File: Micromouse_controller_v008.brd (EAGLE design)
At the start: 50.8 x 43.2 mm, 17 parts, among them IC2 TA4805BF, U1 ATMEGA328P_TQFP

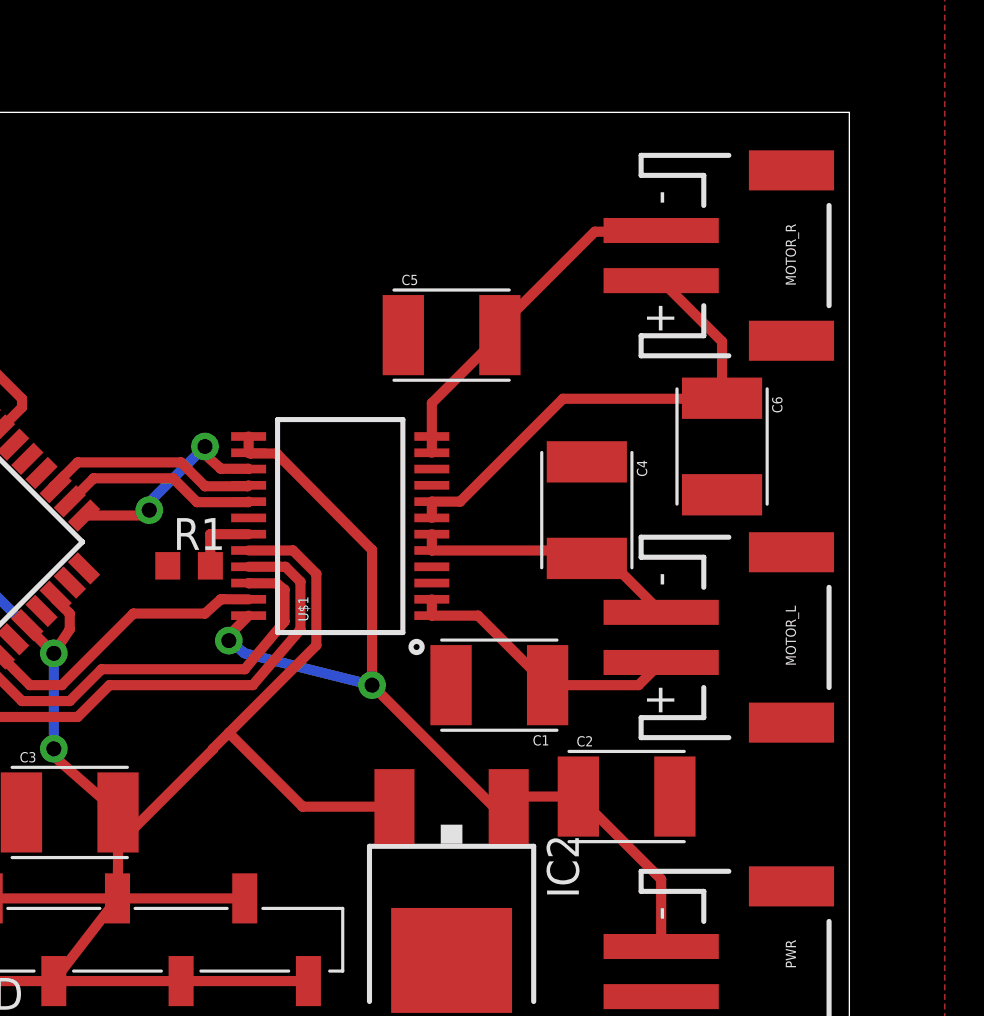
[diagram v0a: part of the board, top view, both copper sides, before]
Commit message: Version 1.0 of Micromouse controller 	Added capacitor values 	Arranged Labels 	Completed BoM and Presentation
Signed-off-by: Matthew Lumantas <mluma001@ucr.edu>
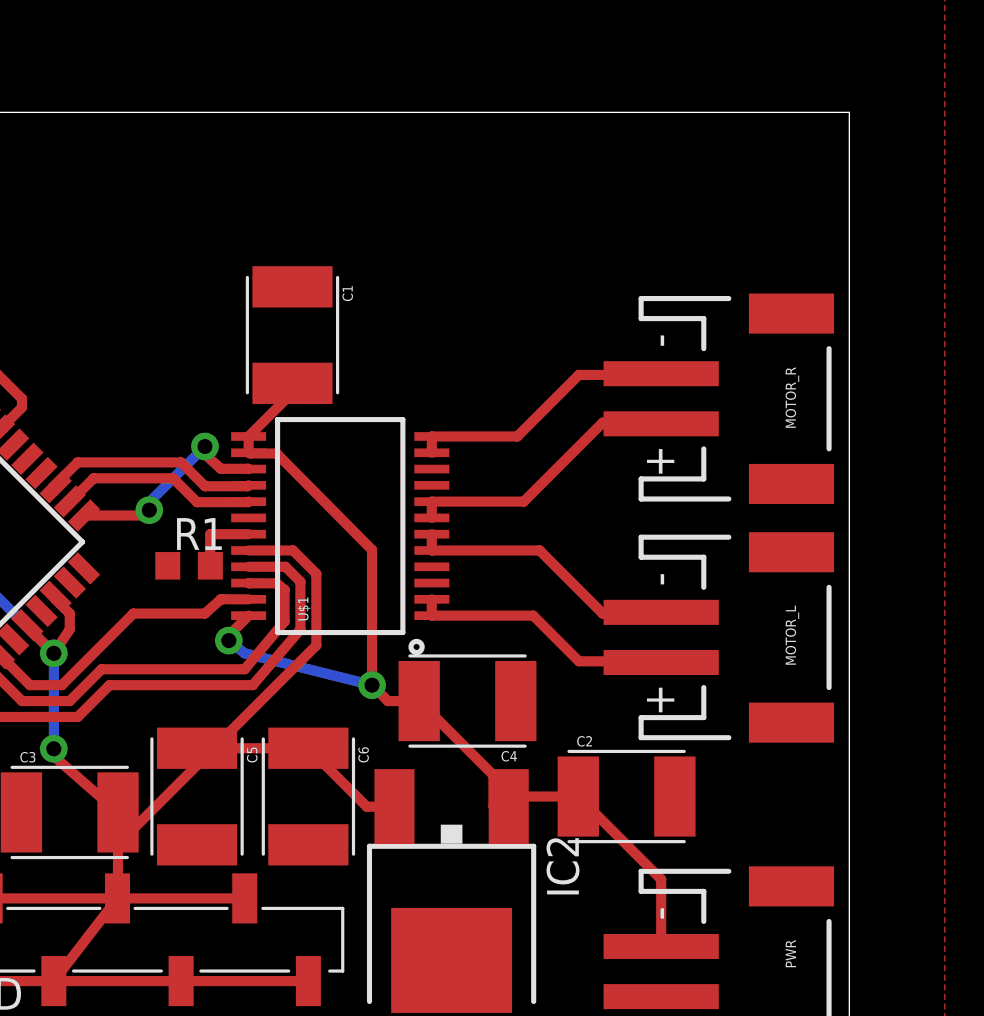
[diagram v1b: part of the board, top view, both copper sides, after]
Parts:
- moved C6 21.6 mm to (29.2, 15.9)
- moved C5 21.0 mm to (24.8, 15.9), turned to 270 degrees
- moved C1 16.2 mm to (28.6, 34.3), turned to 270 degrees
- moved C4 8.99 mm to (35.6, 19.7), turned to 180 degrees
- moved MOTOR_R 5.72 mm to (47.0, 31.8)
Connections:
- net +12V: now also C1.A, C4.A
- net +5V: now also C5.C, C6.C
- net GND: now also C1.C, C5.A; no longer C1.A, C5.C
- net N$11: no longer C1.C
- net N$12: no longer C4.A
- net N$13: no longer C5.A
- net N$14: no longer C6.C
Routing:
- net N$14: track 19.6 -> 11.1 mm
- net +12V: track 37.7 -> 41.3 mm
- net N$13: track 14.2 -> 10.8 mm
- net +5V: track 97.2 -> 98.5 mm
- net N$11: track 11.3 -> 10.6 mm
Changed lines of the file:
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@@
 <attribute name="PROD_ID" value="CONN-11443" x="46.99" y="22.225" size="1.778" layer="27" rot="R270" display="off"/>
 </element>
-<element name="MOTOR_R" library="SparkFun-Connectors" package="JST-2-SMD" value="" x="46.99" y="37.465" rot="R270">
-<attribute name="PROD_ID" value="CONN-11443" x="46.99" y="37.465" size="1.778" layer="27" rot="R270" display="off"/>
+<element name="MOTOR_R" library="SparkFun-Connectors" package="JST-2-SMD" value="" x="46.99" y="31.75" rot="R270">
+<attribute name="PROD_ID" value="CONN-11443" x="46.99" y="31.75" size="1.778" layer="27" rot="R270" display="off"/>
 </element>
 <element name="U$1" library="SparkFun-PowerIC" package="SSOP24" value="TB6612FNG" x="30.48" y="26.67" rot="R90">
@@
 <element name="R1" library="resistor" package="R0603" value="10k" x="24.4475" y="25.0825"/>
 <element name="IC2" library="Micromouse" package="DPAK" value="TA4805BF" x="34.925" y="11.43" rot="R180"/>
-<element name="C1" library="SparkFun-Capacitors" package="GRM43D" value="" x="36.83" y="20.32" rot="R180"/>
-<element name="C4" library="SparkFun-Capacitors" package="GRM43D" value="" x="40.3225" y="27.305" rot="R270"/>
-<element name="C5" library="SparkFun-Capacitors" package="GRM43D" value="" x="34.925" y="34.29"/>
-<element name="C6" library="SparkFun-Capacitors" package="GRM43D" value="" x="45.72" y="29.845" rot="R270"/>
+<element name="C1" library="SparkFun-Capacitors" package="GRM43D" value="" x="28.575" y="34.29" rot="R270"/>
+<element name="C4" library="SparkFun-Capacitors" package="GRM43D" value="" x="35.56" y="19.685" rot="R180"/>
+<element name="C5" library="SparkFun-Capacitors" package="GRM43D" value="" x="24.765" y="15.875" rot="R270"/>
+<element name="C6" library="SparkFun-Capacitors" package="GRM43D" value="" x="29.21" y="15.875" rot="R270"/>
 </elements>
 <signals>
@@
 <contactref element="JP1" pad="6"/>
 <contactref element="R1" pad="1"/>
-<contactref element="C6" pad="A"/>
-<contactref element="C1" pad="A"/>
-<contactref element="C5" pad="C"/>
-<contactref element="C4" pad="C"/>
 <contactref element="C3" pad="C"/>
 <contactref element="C2" pad="A"/>
 <contactref element="IC2" pad="4"/>
+<contactref element="C1" pad="C"/>
+<contactref element="C4" pad="C"/>
+<contactref element="C5" pad="A"/>
+<contactref element="C6" pad="A"/>
 </signal>
 <signal name="N$11">
@@
 <contactref element="MOTOR_L" pad="2"/>
 <wire x1="34.136" y1="23.745" x2="34.136" y2="23.095" width="0.4064" layer="1"/>
-<contactref element="C1" pad="C"/>
-<wire x1="34.136" y1="23.095" x2="35.982" y2="23.095" width="0.4064" layer="1"/>
-<wire x1="35.982" y1="23.095" x2="38.757" y2="20.32" width="0.4064" layer="1"/>
-<wire x1="38.757" y1="20.32" x2="42.385" y2="20.32" width="0.4064" layer="1"/>
-<wire x1="42.385" y1="20.32" x2="43.29" y2="21.225" width="0.4064" layer="1"/>
+<wire x1="34.136" y1="23.095" x2="38.1825" y2="23.095" width="0.4064" layer="1"/>
+<wire x1="38.1825" y1="23.095" x2="40.005" y2="21.2725" width="0.4064" layer="1"/>
+<wire x1="40.005" y1="21.2725" x2="43.2425" y2="21.2725" width="0.4064" layer="1"/>
+<wire x1="43.2425" y1="21.2725" x2="43.29" y2="21.225" width="0.4064" layer="1"/>
 </signal>
 <signal name="N$12">
@@
 <contactref element="MOTOR_L" pad="1"/>
 <wire x1="34.136" y1="26.345" x2="34.136" y2="25.695" width="0.4064" layer="1"/>
-<contactref element="C4" pad="A"/>
-<wire x1="34.136" y1="25.695" x2="39.688" y2="25.695" width="0.4064" layer="1"/>
-<wire x1="39.688" y1="25.695" x2="40.3225" y2="25.378" width="0.4064" layer="1"/>
-<wire x1="40.3225" y1="25.378" x2="41.137" y2="25.378" width="0.4064" layer="1"/>
-<wire x1="41.137" y1="25.378" x2="43.29" y2="23.225" width="0.4064" layer="1"/>
+<wire x1="34.136" y1="25.695" x2="38.44" y2="25.695" width="0.4064" layer="1"/>
+<wire x1="38.44" y1="25.695" x2="40.9575" y2="23.1775" width="0.4064" layer="1"/>
+<wire x1="40.9575" y1="23.1775" x2="43.2425" y2="23.1775" width="0.4064" layer="1"/>
+<wire x1="43.2425" y1="23.1775" x2="43.29" y2="23.225" width="0.4064" layer="1"/>
 </signal>
 <signal name="N$13">
@@
 <contactref element="U$1" pad="11"/>
 <wire x1="34.136" y1="29.595" x2="34.136" y2="30.245" width="0.4064" layer="1"/>
-<contactref element="C5" pad="A"/>
-<wire x1="34.136" y1="30.245" x2="34.136" y2="31.574" width="0.4064" layer="1"/>
-<wire x1="34.136" y1="31.574" x2="36.852" y2="34.29" width="0.4064" layer="1"/>
-<wire x1="36.852" y1="34.29" x2="36.852" y2="34.6295" width="0.4064" layer="1"/>
-<wire x1="36.852" y1="34.6295" x2="40.64" y2="38.4175" width="0.4064" layer="1"/>
-<wire x1="40.64" y1="38.4175" x2="43.2425" y2="38.4175" width="0.4064" layer="1"/>
-<wire x1="43.2425" y1="38.4175" x2="43.29" y2="38.465" width="0.4064" layer="1"/>
+<wire x1="34.136" y1="30.245" x2="37.5475" y2="30.245" width="0.4064" layer="1"/>
+<wire x1="37.5475" y1="30.245" x2="40.005" y2="32.7025" width="0.4064" layer="1"/>
+<wire x1="40.005" y1="32.7025" x2="43.2425" y2="32.7025" width="0.4064" layer="1"/>
+<wire x1="43.2425" y1="32.7025" x2="43.29" y2="32.75" width="0.4064" layer="1"/>
 </signal>
 <signal name="N$14">
@@
 <contactref element="U$1" pad="8"/>
 <wire x1="34.136" y1="26.995" x2="34.136" y2="27.645" width="0.4064" layer="1"/>
-<contactref element="C6" pad="C"/>
-<wire x1="34.136" y1="27.645" x2="35.265" y2="27.645" width="0.4064" layer="1"/>
-<wire x1="35.265" y1="27.645" x2="39.37" y2="31.75" width="0.4064" layer="1"/>
-<wire x1="39.37" y1="31.75" x2="45.698" y2="31.75" width="0.4064" layer="1"/>
-<wire x1="45.698" y1="31.75" x2="45.72" y2="31.772" width="0.4064" layer="1"/>
-<wire x1="45.72" y1="31.772" x2="45.72" y2="34.035" width="0.4064" layer="1"/>
-<wire x1="45.72" y1="34.035" x2="43.29" y2="36.465" width="0.4064" layer="1"/>
+<wire x1="34.136" y1="27.645" x2="37.805" y2="27.645" width="0.4064" layer="1"/>
+<wire x1="37.805" y1="27.645" x2="40.9575" y2="30.7975" width="0.4064" layer="1"/>
+<wire x1="40.9575" y1="30.7975" x2="43.2425" y2="30.7975" width="0.4064" layer="1"/>
+<wire x1="43.2425" y1="30.7975" x2="43.29" y2="30.75" width="0.4064" layer="1"/>
 </signal>
 <signal name="PWMB_DRIVER">
@@
 <wire x1="37.61" y1="15.875" x2="37.205" y2="15.47" width="0.4064" layer="1"/>
 <wire x1="37.205" y1="15.47" x2="36.6" y2="15.47" width="0.4064" layer="1"/>
-<wire x1="36.6" y1="15.47" x2="31.75" y2="20.32" width="0.4064" layer="1"/>
+<contactref element="C1" pad="A"/>
+<contactref element="C4" pad="A"/>
+<wire x1="36.6" y1="15.47" x2="36.6" y2="16.718" width="0.4064" layer="1"/>
+<wire x1="36.6" y1="16.718" x2="33.633" y2="19.685" width="0.4064" layer="1"/>
+<wire x1="33.633" y1="19.685" x2="32.385" y2="19.685" width="0.4064" layer="1"/>
+<wire x1="32.385" y1="19.685" x2="31.75" y2="20.32" width="0.4064" layer="1"/>
+<wire x1="28.575" y1="32.363" x2="28.575" y2="31.996" width="0.4064" layer="1"/>
+<wire x1="28.575" y1="31.996" x2="26.824" y2="30.245" width="0.4064" layer="1"/>
 </signal>
 <signal name="+5V">
@@
 <wire x1="28.5975" y1="25.695" x2="29.5275" y2="24.765" width="0.4064" layer="1"/>
 <wire x1="29.5275" y1="24.765" x2="29.5275" y2="21.9075" width="0.4064" layer="1"/>
-<wire x1="29.5275" y1="21.9075" x2="26.035" y2="18.415" width="0.4064" layer="1"/>
+<wire x1="29.5275" y1="21.9075" x2="25.422" y2="17.802" width="0.4064" layer="1"/>
 <contactref element="IC2" pad="3"/>
-<wire x1="32.645" y1="15.47" x2="28.98" y2="15.47" width="0.4064" layer="1"/>
-<wire x1="28.98" y1="15.47" x2="26.035" y2="18.415" width="0.4064" layer="1"/>
-<wire x1="25.4" y1="17.78" x2="26.035" y2="18.415" width="0.4064" layer="1"/>
+<wire x1="25.4" y1="17.78" x2="24.765" y2="17.145" width="0.4064" layer="1"/>
 <wire x1="25.4" y1="17.78" x2="25.4" y2="17.758" width="0.4064" layer="1"/>
 <wire x1="25.4" y1="17.758" x2="21.612" y2="13.97" width="0.4064" layer="1"/>
+<contactref element="C5" pad="C"/>
+<contactref element="C6" pad="C"/>
+<wire x1="32.645" y1="15.47" x2="31.542" y2="15.47" width="0.4064" layer="1"/>
+<wire x1="31.542" y1="15.47" x2="29.21" y2="17.802" width="0.4064" layer="1"/>
+<wire x1="29.21" y1="17.802" x2="25.422" y2="17.802" width="0.4064" layer="1"/>
+<wire x1="25.422" y1="17.802" x2="25.4" y2="17.78" width="0.4064" layer="1"/>
+<wire x1="25.4" y1="17.78" x2="24.765" y2="17.802" width="0" layer="19" extent="1-1"/>
 </signal>
 <signal name="N$17">
